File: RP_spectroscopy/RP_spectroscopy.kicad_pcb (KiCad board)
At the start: 2 copper layers, 99 parts, among them IC1 TL081CDR, IC2 TL081CDR, IC3 TL081CDR, J1 Extension connector 1, J10 Conn_Coaxial, J11 Conn_01x04_MountingPin, J2 Extension connector 2, J3 Conn_Coaxial, J4 Conn_Coaxial, J5 Conn_Coaxial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

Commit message: Started to implement the PCB
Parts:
- moved C14 113.3 mm to (277.8, 73.8)
- moved C15 113.3 mm to (277.8, 76.8)
- moved D1 113.3 mm to (229.9, 63.4)
- moved FB1 113.3 mm to (237.3, 29.5)
- moved FB3 113.3 mm to (237.3, 32.0)
- moved FB4 113.3 mm to (237.3, 34.5)
- moved IC1 113.3 mm to (273.4, 35.7)
- moved J3 113.3 mm to (224.2, 22.6)
- moved J5 113.3 mm to (224.2, 49.0)
- moved J6 113.3 mm to (224.2, 62.3)
- moved R27 113.3 mm to (266.7, 33.9)
- moved R28 113.3 mm to (266.7, 36.8)
- moved R31 113.3 mm to (266.7, 45.7)
- moved R32 113.3 mm to (266.7, 48.6)
- moved R33 113.3 mm to (266.7, 51.6)
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
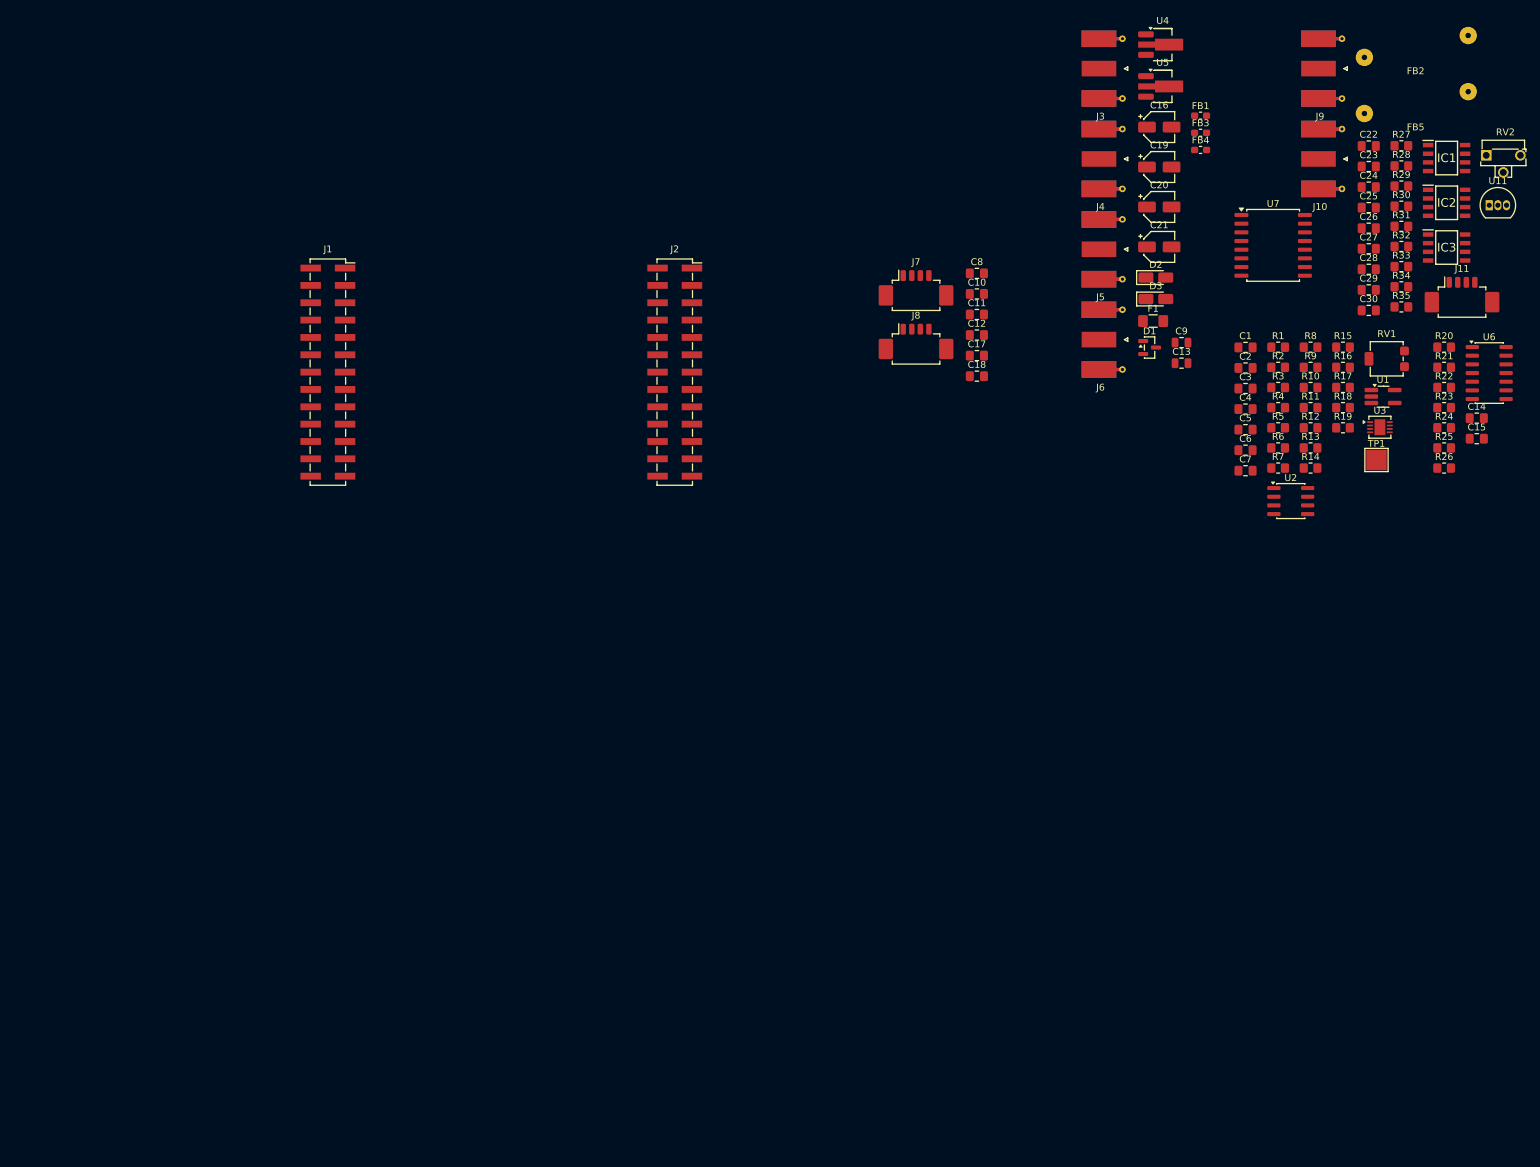
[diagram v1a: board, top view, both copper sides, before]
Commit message: Started to place all the components on the PCB. Simulated a bunch of filters.
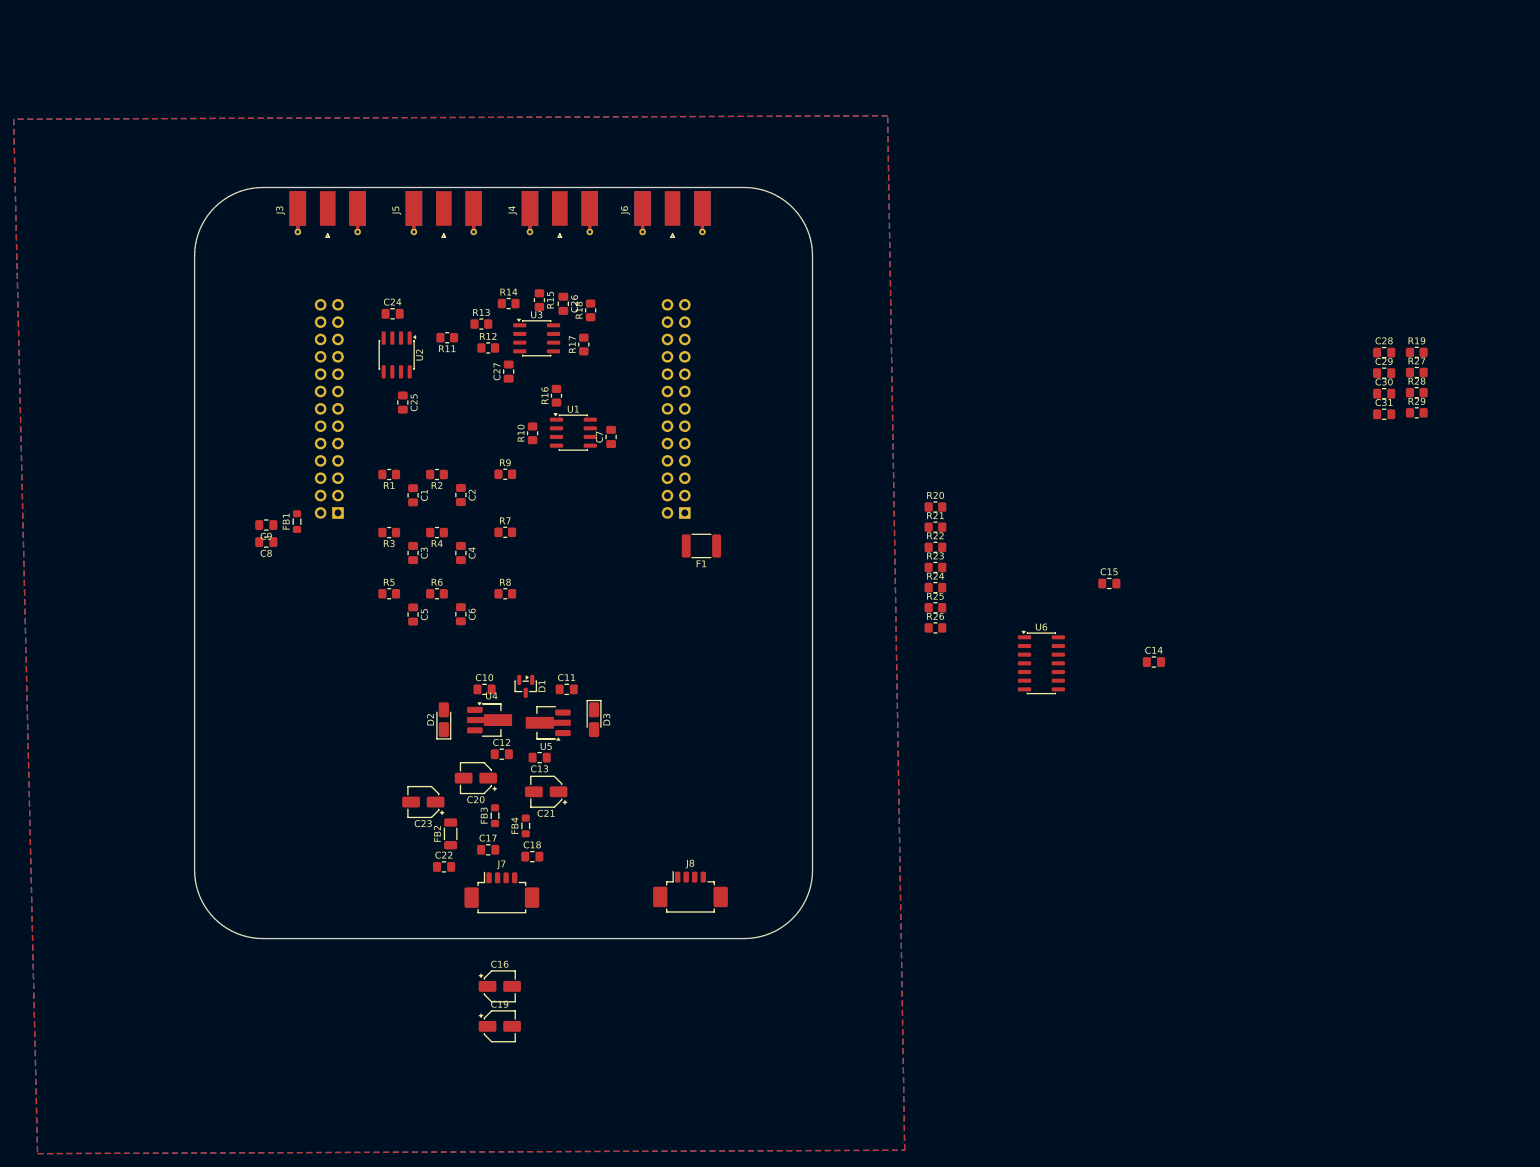
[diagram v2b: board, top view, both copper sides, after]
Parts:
- removed FB5: FerriteBead, Ferrite_THT:FerriteBread
- removed IC1, IC2, IC3: TL081CDR, Library:TL081CDR - SOIC8
- removed J10, J9: Conn_Coaxial, Connector_Coaxial:SMA_Molex_73251-1153_EdgeMount_Horizontal
- removed J11: Conn_01x04_MountingPin, Connector_Molex:Molex_PicoBlade_53261-0471_1x04-1MP_P1.25mm_Horizontal
- removed R30, R33, R34, R35: 10k, Resistor_SMD:R_0805_2012Metric_Pad1.20x1.40mm_HandSolder
- removed R31: 220, Resistor_SMD:R_0805_2012Metric_Pad1.20x1.40mm_HandSolder
- removed R32: 4k7, Resistor_SMD:R_0805_2012Metric_Pad1.20x1.40mm_HandSolder
- removed RV1: 20k, Potentiometer_SMD:Potentiometer_Bourns_3224G_Horizontal
- removed RV2: 50k, Potentiometer_THT:Potentiometer_Runtron_RM-063_Horizontal
- removed TP1: TestPoint_Flag, TestPoint:TestPoint_Pad_3.0x3.0mm
- removed U11: TL431LPG, Package_TO_SOT_THT:TO-92_Inline
- removed U7: INA114BU, Package_SO:SOIC-16W_7.5x10.3mm_P1.27mm
- added C31: 33n, Capacitor_SMD:C_0805_2012Metric_Pad1.18x1.45mm_HandSolder, F.Cu at (264.2, 73.2)
- C13, C9: footprint Capacitor_SMD:C_0805_2012Metric -> Capacitor_SMD:C_0805_2012Metric_Pad1.18x1.45mm_HandSolder
- C22: value 100n -> 1µ
- C23: value 100n -> 10µ; footprint Capacitor_SMD:C_0805_2012Metric_Pad1.18x1.45mm_HandSolder -> Capacitor_SMD:CP_Elec_4x5.3
- C28, C29, C30: value 100n -> 33n
- C7: value 2.2µ -> 100n
- F1: footprint Fuse:Fuse_1206_3216Metric_Pad1.42x1.75mm_HandSolder -> Fuse:Fuse_1812_4532Metric_Pad1.30x3.40mm_HandSolder
- FB1, FB3, FB4: footprint Inductor_SMD:L_0603_1608Metric_Pad1.05x0.95mm_HandSolder -> Inductor_SMD:L_0805_2012Metric_Pad1.05x1.20mm_HandSolder
- FB2: value FerriteBead -> HI1206P121R-10; footprint Ferrite_THT:FerriteBread -> Inductor_SMD:L_1206_3216Metric_Pad1.22x1.90mm_HandSolder
- J1, J2: footprint Connector_PinSocket_2.54mm:PinSocket_2x13_P2.54mm_Vertical_SMD -> Connector_PinSocket_2.54mm:PinSocket_2x13_P2.54mm_Vertical; moved to B.Cu
- R19: value 1k -> 2K55
- R27: value 10k -> 365
- R28: value 10k -> 1K05
- R29: value 10k -> 887
- U1: footprint Package_TO_SOT_SMD:TSOT-23-5_HandSoldering -> Package_SO:SOIC-8_3.9x4.9mm_P1.27mm
- U3: footprint Package_CSP:LFCSP-8-1EP_3x3mm_P0.5mm_EP1.6x2.34mm -> Package_SO:SOIC-8_3.9x4.9mm_P1.27mm
- moved FB2 179.8 mm to (127.5, 134.7), turned to 90 degrees
- moved C22 171.7 mm to (126.5, 139.5)
- moved C23 166.8 mm to (123.5, 130.0), turned to 180 degrees
- moved C16 158.6 mm to (134.7, 157.0)
- moved C19 158.6 mm to (134.7, 162.8)
- moved FB1 145.1 mm to (105.0, 88.9), turned to 90 degrees
- moved C25 144.3 mm to (120.5, 71.5), turned to -90 degrees
- moved C24 144.2 mm to (119.0, 58.5)
- moved FB3 143.8 mm to (134.0, 132.0), turned to 90 degrees
- moved FB4 139.9 mm to (138.5, 133.5), turned to 90 degrees
- moved U4 139.4 mm to (133.5, 118.0)
- moved C9 136.7 mm to (100.5, 89.4), turned to 180 degrees
- moved U2 132.7 mm to (119.6, 64.5), turned to -90 degrees
- moved R5 132.4 mm to (118.5, 99.5)
- moved R3 131.9 mm to (118.5, 90.5), turned to 180 degrees
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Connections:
- C20 pad 1: GND -> Net-(D2-K)
- C20 pad 2: Net-(D2-K) -> GND
- C22 pad 1: -12V -> GND
- C22 pad 2: GND -> Net-(J7-Pin_1)
- C23 pad 1: +12V -> +5V
- C24 pad 1: Net-(U7-FEEDBACK) -> +5VA
- C24 pad 2: Net-(IC1-IN+) -> GND
- C25 pad 1: -12V -> -5VA
- C26 pad 1: +12V -> GND
- C26 pad 2: GND -> +5VA
- C27 pad 1: -12V -> GND
- C27 pad 2: GND -> -5VA
- C28 pad 1: +12V -> PD
- C28 pad 2: GND -> Net-(C28-Pad2)
- C29 pad 1: -12V -> Net-(C28-Pad2)
- C29 pad 2: GND -> Net-(C29-Pad2)
- C30 pad 1: +12V -> Net-(C30-Pad1)
- C30 pad 2: GND -> Net-(C30-Pad2)
- C7 pad 1: Net-(C7-Pad1) -> +3V3
- FB2 pad 1: Net-(J11-Pin_4) -> Net-(J7-Pin_1)
- FB2 pad 2: -12V -> +5V
- J1 pad 5: unconnected-(J1-Pin_5-Pad5) -> Ramp sign
- J2 pad 20: unconnected-(J2-Pin_20-Pad20) -> Not used
- J7 pad 1: unconnected-(J7-Pin_1-Pad1) -> Net-(J7-Pin_1)
- J7 pad 3: unconnected-(J7-Pin_3-Pad3) -> GND
- R19 pad 1: +3V3 -> Net-(C29-Pad2)
- R19 pad 2: Net-(C7-Pad1) -> GND
- R27 pad 1: Net-(R27-Pad1) -> Net-(C28-Pad2)
- R27 pad 2: Net-(R27-Pad2) -> Net-(C30-Pad1)
- R29 pad 1: Net-(J9-In) -> Net-(C30-Pad2)
- R29 pad 2: GND -> unconnected-(R29-Pad2)
- U1 pad 3: Net-(U1-+) -> GND
- U2 pad 6: unconnected-(U2-Pad6) -> Ramp sign
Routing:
- added copper zone on B.Cu, net GND
- added copper zone on F.Cu, net GND
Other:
- board outline added: 90.5 x 110 mm

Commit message: Additional modifications of parameters for produciton and some footprints
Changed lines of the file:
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@@
 			(pintype "passive")
 		)
-		(pad "19" thru_hole circle
+		(pad "19" thru_hole oval
 			(at 0 -22.86)
-			(size 1.7 1.7)
+			(size 2.2 1.7)
 			(drill 1)
 			(layers "*.Cu" "*.Mask")

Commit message: Check of the availability of all the components and of the footprints. Added the demultiplexer part of the circuit. Some graphical changes. Changed the values of some R in order to match the ones available in the officina elettronica.
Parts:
- C16, C19, C20, C21, C23: footprint Capacitor_SMD:CP_Elec_4x5.3 -> Capacitor_SMD:CP_Elec_6.3x5.7
- FB1: footprint Inductor_SMD:L_0805_2012Metric_Pad1.05x1.20mm_HandSolder -> Inductor_SMD:L_0603_1608Metric_Pad1.05x0.95mm_HandSolder
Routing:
- net Small offset: track 0.00 -> 3.65 mm
